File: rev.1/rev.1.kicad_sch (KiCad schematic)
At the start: 0 parts

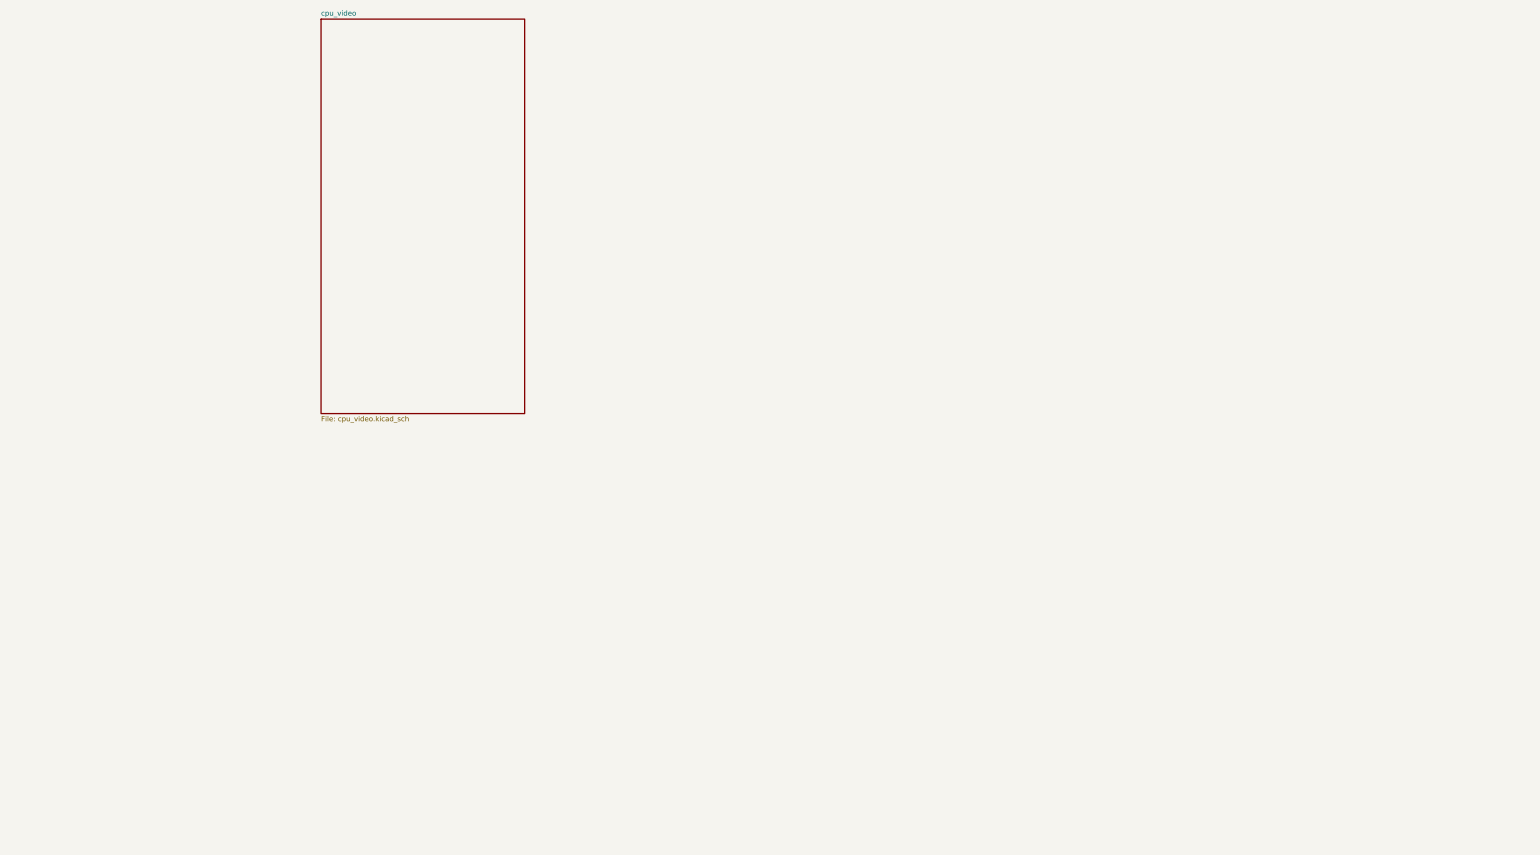
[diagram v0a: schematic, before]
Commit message: убрал иерархию
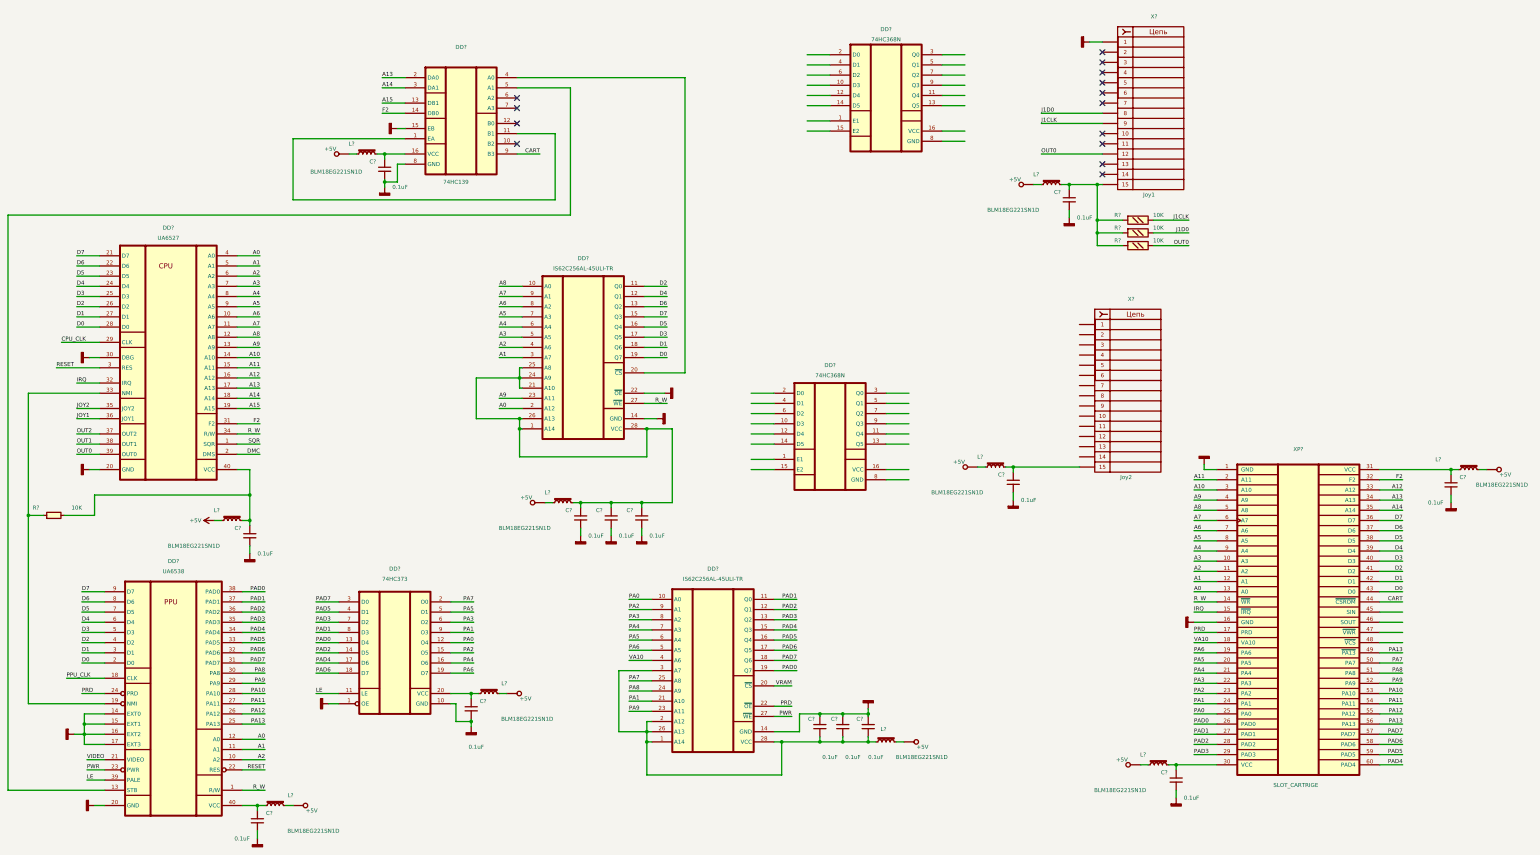
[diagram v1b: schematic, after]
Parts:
- added C? (x14): 0.1uF, symbol Device:C_Small
- added DD? (x2): 74HC368N, symbol 74xx:74HC368N_gost
- added DD? (x2): IS62C256AL-45ULI-TR, symbol Memory_RAM:IS62C256AL-45ULI-TR
- added DD?: 74HC373, symbol 74xx:74HC373_gost
- added DD?: 74HC139, symbol 74xx:74HC139N_gost
- added DD?: UA6527, symbol CPU:UA6527
- added DD?: UA6538, symbol Video:UA6538
- added L? (x10): BLM18EG221SN1D, symbol Device:L_Iron_Small
- added R? (x3): 10K, symbol Resistor_gost:R_125
- added R?: 10K, symbol Device:R_Small
- added X?: Joy1, symbol Connectors_gost:Conn_01x15_Female
- added X?: Joy2, symbol Connectors_gost:Conn_01x15_Female
- added XP?: SLOT_CARTRIGE, symbol Connector_Generic:Conn_02x30_Top_Bottom_dendy
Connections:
- new net: C?.1, C?.1, C?.1, DD?.1 (A14), DD?.21 (A10), DD?.24 (A9), DD?.25 (A8), DD?.26 (A13), DD?.28 (VCC), L?.2
- new net: DD?.20 (~{CS}), DD?.4 (A0)
- new net: C?.1, L?.2, R?.2, R?.2, R?.2, X?.15 (Pin_15)
- new net: C?.1, C?.1, C?.1, DD?.1 (A14), DD?.2 (A12), DD?.26 (A13), DD?.28 (VCC), DD?.3 (A7), L?.2
- new net: C?.1, DD?.16 (VCC), L?.2
- new net: C?.1, DD?.20 (VCC), L?.2
- new net: C?.1, DD?.40 (VCC), L?.2, R?.2
- new net: C?.1, L?.2, X?.15 (Pin_15)
- new net: C?.1, L?.2, XP?.31 (VCC)
- new net: C?.1, DD?.40 (VCC), L?.2
- new net: DD?.1 (EA), DD?.11 (B1)
- new net: DD?.13 (STB), DD?.5 (A1)
- new net: C?.1, L?.2, XP?.30 (VCC)
- new net: DD?.19 (NMI), DD?.33 (NMI), R?.1
- new net +5V: L?.1, L?.1, L?.1, L?.1, L?.1, L?.1, L?.1, L?.1, L?.1, L?.1
- new net A0: DD?.12 (A0), DD?.2 (A12), DD?.4 (A0), XP?.13 (A0)
- new net A1: DD?.11 (A1), DD?.3 (A7), DD?.5 (A1), XP?.12 (A1)
- new net A10: DD?.14 (A10), XP?.3 (A10)
- new net A11: DD?.15 (A11), XP?.2 (A11)
- new net A12: DD?.16 (A12), XP?.33 (A12)
- new net A13: DD?.17 (A13), DD?.2 (DA0), XP?.34 (A13)
- new net A14: DD?.18 (A14), DD?.3 (DA1), XP?.35 (A14)
- new net A15: DD?.13 (DB1), DD?.19 (A15)
- new net A2: DD?.10 (A2), DD?.4 (A6), DD?.6 (A2), XP?.11 (A2)
- new net A3: DD?.5 (A5), DD?.7 (A3), XP?.10 (A3)
- new net A4: DD?.6 (A4), DD?.8 (A4), XP?.9 (A4)
- new net A5: DD?.7 (A3), DD?.9 (A5), XP?.8 (A5)
- new net A6: DD?.10 (A6), DD?.8 (A2), XP?.7 (A6)
- new net A7: DD?.11 (A7), DD?.9 (A1), XP?.6 (A7)
- new net A8: DD?.10 (A0), DD?.12 (A8), XP?.5 (A8)
- new net A9: DD?.13 (A9), DD?.23 (A11), XP?.4 (A9)
- new net CART: DD?.9 (B3), XP?.44 (~{CSROM})
- new net CPU_CLK: DD?.29 (CLK)
- new net D0: DD?.19 (Q7), DD?.2 (D0), DD?.28 (D0), XP?.43 (D0)
- new net D1: DD?.18 (Q6), DD?.27 (D1), DD?.3 (D1), XP?.42 (D1)
- new net D2: DD?.11 (Q0), DD?.26 (D2), DD?.4 (D2), XP?.41 (D2)
- new net D3: DD?.17 (Q5), DD?.25 (D3), DD?.5 (D3), XP?.40 (D3)
- new net D4: DD?.12 (Q1), DD?.24 (D4), DD?.6 (D4), XP?.39 (D4)
- new net D5: DD?.16 (Q4), DD?.23 (D5), DD?.7 (D5), XP?.38 (D5)
- new net D6: DD?.13 (Q2), DD?.22 (D6), DD?.8 (D6), XP?.37 (D6)
- new net D7: DD?.15 (Q3), DD?.21 (D7), DD?.9 (D7), XP?.36 (D7)
- new net DMC: DD?.2 (DMS)
- new net F2: DD?.14 (DB0), DD?.31 (F2), XP?.32 (F2)
- new net GNDD: C?.2, C?.2, C?.2, C?.2, C?.2, C?.2, C?.2, C?.2, C?.2, C?.2, C?.2, C?.2, C?.2, C?.2, DD?.1 (OE), DD?.10 (GND), DD?.14 (EXT0), DD?.14 (GND), DD?.14 (GND), DD?.15 (EB), DD?.15 (EXT1), DD?.16 (EXT2), DD?.17 (EXT3), DD?.20 (GND), DD?.20 (GND), DD?.22 (~{OE}), DD?.30 (DBG), DD?.8 (GND), X?.1 (Pin_1), XP?.1 (GND), XP?.16 (GND)
- new net IRQ: DD?.32 (IRQ), XP?.15 (~{IRQ})
- new net J1CLK: R?.1, X?.9 (Pin_9)
- new net J1D0: R?.1, X?.8 (Pin_8)
- new net JOY1: DD?.36 (JOY1)
- new net JOY2: DD?.35 (JOY2)
- new net LE: DD?.11 (LE), DD?.39 (PALE)
- new net OUT0: DD?.39 (OUT0), R?.1, X?.12 (Pin_12)
- new net OUT1: DD?.38 (OUT1)
- new net OUT2: DD?.37 (OUT2)
- new net PA0: DD?.10 (A0), DD?.12 (O4), XP?.25 (PA0)
- new net PA1: DD?.21 (A10), DD?.9 (O3), XP?.24 (PA1)
- new net PA10: DD?.28 (PA10), XP?.53 (PA10)
- new net PA11: DD?.27 (PA11), XP?.54 (PA11)
- new net PA12: DD?.26 (PA12), XP?.55 (PA12)
- new net PA13: DD?.25 (PA13), XP?.49 (~{PA13}), XP?.56 (PA13)
- new net PA2: DD?.15 (O5), DD?.9 (A1), XP?.23 (PA2)
- new net PA3: DD?.6 (O2), DD?.8 (A2), XP?.22 (PA3)
- new net PA4: DD?.16 (O6), DD?.7 (A3), XP?.21 (PA4)
- new net PA5: DD?.5 (O1), DD?.6 (A4), XP?.20 (PA5)
- new net PA6: DD?.19 (O7), DD?.5 (A5), XP?.19 (PA6)
- new net PA7: DD?.2 (O0), DD?.25 (A8), XP?.50 (PA7)
- new net PA8: DD?.24 (A9), DD?.30 (PA8), XP?.51 (PA8)
- new net PA9: DD?.23 (A11), DD?.29 (PA9), XP?.52 (PA9)
- new net PAD0: DD?.13 (D4), DD?.19 (Q7), DD?.38 (PAD0), XP?.26 (PAD0)
- new net PAD1: DD?.11 (Q0), DD?.37 (PAD1), DD?.8 (D3), XP?.27 (PAD1)
- new net PAD2: DD?.12 (Q1), DD?.14 (D5), DD?.36 (PAD2), XP?.28 (PAD2)
- new net PAD3: DD?.13 (Q2), DD?.35 (PAD3), DD?.7 (D2), XP?.29 (PAD3)
- new net PAD4: DD?.15 (Q3), DD?.17 (D6), DD?.34 (PAD4), XP?.60 (PAD4)
- new net PAD5: DD?.16 (Q4), DD?.33 (PAD5), DD?.4 (D1), XP?.59 (PAD5)
- new net PAD6: DD?.17 (Q5), DD?.18 (D7), DD?.32 (PAD6), XP?.58 (PAD6)
- new net PAD7: DD?.18 (Q6), DD?.3 (D0), DD?.31 (PAD7), XP?.57 (PAD7)
- new net PPU_CLK: DD?.18 (CLK)
- new net PRD: DD?.22 (~{OE}), DD?.24 (PRD), XP?.17 (PRD)
- new net PWR: DD?.23 (PWR), DD?.27 (~{WE})
- new net RESET: DD?.22 (RES), DD?.3 (RES)
- new net R_W: DD?.1 (R/W), DD?.27 (~{WE}), DD?.34 (R/W), XP?.14 (~{WR})
- new net SQR: DD?.1 (SQR)
- new net VA10: DD?.4 (A6), XP?.18 (VA10)
- new net VIDEO: DD?.21 (VIDEO)
- new net VRAM: DD?.20 (~{CS})
- no-connect marks 0 -> 14
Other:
- removed sheet cpu_video

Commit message: добавил документацию опринципах работы приставки и доделал джойстики
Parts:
- removed C?: 0.1uF, symbol Device:C_Small
- removed L?: BLM18EG221SN1D, symbol Device:L_Iron_Small
- removed R? (x2): 10K, symbol Resistor_gost:R_125
- removed X?: Joy1, symbol Connectors_gost:Conn_01x15_Female
- removed X?: Joy2, symbol Connectors_gost:Conn_01x15_Female
- added C? (x3): 0.1uF, symbol Device:C_Small
- added L? (x3): BLM18EG221SN1D, symbol Device:L_Iron_Small
- added R? (x11): 10K, symbol Resistor_gost:R_125
- added X?: Манипулятор_2, symbol Connectors_gost:DB15_Female_HighDensity_gost
- added X?: Манипулятор_1, symbol Connectors_gost:DB15_Female_HighDensity_gost
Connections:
- net +5V: now also L?.1, L?.1, L?.1
- net D0: now also DD?.13 (Q5), DD?.3 (Q0)
- net D1: now also DD?.5 (Q1), DD?.5 (Q1)
- net D2: now also DD?.11 (Q4), DD?.9 (Q3)
- net D3: now also DD?.7 (Q2)
- net D4: now also DD?.9 (Q3)
- net F2: now also DD?.2 (D0), DD?.6 (D2)
- net GNDD: now also DD?.10 (D3), DD?.15 (E2), DD?.8 (GND), DD?.8 (GND), C?.2, C?.2, C?.2, X?.1, X?.1
- net IRQ: now also R?.1, X?.3
- net J1CLK: now also DD?.7 (Q2), R?.1, X?.14, X?.9; no longer R?.1
- net J1D0: now also DD?.2 (D0), R?.1, X?.2, X?.8
- net JOY1: now also DD?.1 (E1)
- net JOY2: now also DD?.1 (E1), DD?.15 (E2)
- net OUT0: now also R?.1, X?.12, X?.12
- net OUT1: now also R?.1, X?.11
- net OUT2: now also R?.1, X?.10
- net PA13: now also DD?.12 (D4); no longer XP?.49 (~{PA13})
- net PWR: now also XP?.47 (~{VWR})
- net VRAM: now also XP?.48 (~{VCS})
- net nPA13: now reaches DD?.11 (Q4)
- net nPA13: now also XP?.49 (~{PA13})
- net at DD?.16 (VCC): now also C?.1, L?.2 (x2)
- net J1D1: now reaches DD?.4 (D1)
- net J1D1: now also X?.13
- net at C?.1, L?.2, R?.2: now also R?.2, R?.2, X?.15
- net J2D4: now reaches DD?.10 (D3)
- net J2D4: now also R?.1, X?.4
- net J2D2: now reaches DD?.12 (D4)
- net J2D2: now also R?.1, X?.6
- net J2D0: now reaches DD?.14 (D5)
- net J2D0: now also R?.1, X?.8
- net J2CLK: now reaches DD?.3 (Q0)
- net J2CLK: now also R?.1, X?.9
- net J2D1: now reaches DD?.4 (D1)
- net J2D1: now also R?.1, X?.7
- net J2D3: now reaches DD?.6 (D2)
- net J2D3: now also R?.1, X?.5
- net at XP?.45 (SIN): now also XP?.46 (SOUT)
- new net: C?.1, L?.2, R?.2, R?.2, R?.2, R?.2, R?.2, R?.2, R?.2, R?.2, R?.2, X?.15
- no-connect marks 14 -> 6
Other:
- moved on the sheet: C?, DD?, L?, R?, XP?

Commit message: добавил видеоусилитель
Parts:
- added C?: 220uFx10V, symbol Device_gost:C_Polarized_Small
- added C? (x10): 330pF, symbol Device:C_Small
- added C?: 0.1uF, symbol Device:C_Small
- added D?: SS14, Diode_SMD_AKL:D_SMA, symbol Diode_Schottky_gost:SS14
- added L?: BLM18EG221SN1D, symbol Device:L_Iron_Small
- added Q?: BC817, Package_TO_SOT_SMD:SOT-23, symbol Transistor_BJT:BC817
- added Q?: BC857, Package_TO_SOT_SMD:SOT-23, symbol Transistor_BJT:BC857
- added R?: 75R, symbol Resistor_gost:R_125
- added R?: 2K2, symbol Resistor_gost:R_125
- added R?: 220R, symbol Resistor_gost:R_125
- added R?: 68R, symbol Resistor_gost:R_125
- added X?: VIDEO, symbol Connectors_gost:Conn_01x04_Female
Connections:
- net +5V: now also L?.1
- net GNDD: now also C?.2, C?.2, C?.2, C?.2, C?.2, C?.2, C?.2, C?.2, C?.2, C?.2, C?.2, Q?.3 (C), R?.1, X?.2 (Pin_2), X?.3 (Pin_3), X?.4 (Pin_4)
- net IRQ: now also C?.1
- net J1CLK: now also C?.1
- net J1D0: now also C?.1
- net J2CLK: now also C?.1
- net J2D0: now also C?.1
- net J2D1: now also C?.1
- net J2D2: now also C?.1
- net J2D3: now also C?.1
- net J2D4: now also C?.1
- net OUT2: now also C?.1
- net VIDEO: now also Q?.1 (B)
- new net: D?.1 (K), Q?.1 (B), R?.1, R?.2
- new net: C?.1, D?.2 (A), Q?.2 (E), R?.2
- new net: C?.2, R?.2
- new net: R?.1, X?.1 (Pin_1)
- new net: C?.1, L?.2, Q?.3 (C), R?.2
- new net: Q?.2 (E), R?.1
- no-connect marks 6 -> 16
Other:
- note added: "ВЫХОД"
- note added: "ЗЕМЛЯ"
- moved on the sheet: C?, L?, XP?

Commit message: добавил генератор частоты на 74ls04
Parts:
- added C?: 0.1uF, symbol Device:C_Small
- added C? (x2): 22pF, symbol Device:C_Small
- added DD?: 74LS04, symbol 74xx:74HC04_gost
- added L?: BLM18EG221SN1D, symbol Device:L_Iron_Small
- added R?: 4M7, symbol Resistor_gost:R_125
- added Z?: 26.601712 Mhz, symbol Device_gost:Crystal_Small
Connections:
- net +5V: now also L?.1
- net CPU_CLK: now also DD?.6 (3Y)
- net GNDD: now also C?.2, C?.2, C?.2, DD?.11 (5A), DD?.13 (6A), DD?.7 (GND), DD?.9 (4A)
- net PPU_CLK: now also DD?.4 (2Y)
- new net: C?.1, DD?.10 (5Y), DD?.12 (6Y), DD?.14 (VCC), DD?.8 (4Y), L?.2
- new net: C?.1, DD?.1 (1A), R?.2, Z?.1
- new net: C?.1, DD?.2 (1Y), DD?.3 (2A), DD?.5 (3A), R?.1, Z?.2

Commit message: закончил схему звукового вывода
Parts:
- added C? (x2): 0.1uF, symbol Device:C_Small
- added C? (x5): 10uFx16V, symbol Device_gost:C_Polarized_Small
- added DA? (x2): LM358, symbol Amplifier_Operational:LM2904_gost
- added L?: BLM18EG221SN1D, symbol Device:L_Iron_Small
- added R? (x6): 4K7, symbol Resistor_gost:R_125
- added R? (x2): 75R, symbol Resistor_gost:R_125
- added R? (x2): 1R, symbol Resistor_gost:R_125
- added R? (x2): 510R, symbol Resistor_gost:R_125
- added R? (x3): 1K, symbol Resistor_gost:R_125
- added R? (x2): 2K, symbol Resistor_gost:R_125
- added R?: 1K8, symbol Resistor_gost:R_125
- added R? (x2): 10K, symbol Resistor_gost:R_125
- added R?: 2K2, symbol Resistor_gost:R_125
- added X?: AUDIO_1, symbol Connectors_gost:Conn_01x04_Female
- added X?: AUDIO_2, symbol Connectors_gost:Conn_01x04_Female
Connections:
- net +5V: now also L?.1
- net DMC: now also R?.1, R?.2, R?.2
- net GNDD: now also C?.2, C?.2, C?.2, DA?.4 (V-), R?.1, R?.1, R?.1, R?.2, R?.2, R?.2, X?.2 (Pin_2), X?.2 (Pin_2), X?.3 (Pin_3), X?.3 (Pin_3), X?.4 (Pin_4), X?.4 (Pin_4)
- net SQR: now also R?.1, R?.2, R?.2
- net SOUT: now reaches XP?.45 (SIN), XP?.46 (SOUT)
- net SOUT: now also R?.1, R?.2, R?.2
- new net: C?.2, R?.1, R?.1, R?.1 (x2)
- new net: C?.1, R?.1 (x2)
- new net: DA?.7, R?.1, R?.2
- new net: C?.1, C?.1, R?.1, R?.2, R?.2, R?.2
- new net: C?.2, X?.1 (Pin_1) (x2)
- new net: DA?.6 (-), R?.1, R?.2
- new net: C?.1, DA?.5 (+), R?.1, R?.2
- new net: C?.1, DA?.3 (+), R?.1, R?.2
- new net: DA?.1, R?.1, R?.2
- new net: DA?.2 (-), R?.1, R?.2
- new net +5VA: C?.1, DA?.8 (V+), L?.2, R?.2, R?.2, R?.2
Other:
- moved on the sheet: C?, D?, DD?, L?, Q?, R?, X?, Z?

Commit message: Добавил стабилизатор питания и закончил схему
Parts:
- added C1: 0.47uF, symbol Device:C_Small
- added C2: 220uFx25V, symbol Device_gost:C_Polarized_Small
- added C6: 470p, symbol Device:C_Small
- added C8: 470uFx6.3V, symbol Device_gost:C_Polarized_Small
- added D1, D2: SS14, Diode_SMD_AKL:D_SMA, symbol Diode_Schottky_gost:SS14
- added D3: POWER, symbol Device:LED_Small
- added DA1: MC34063AD, Package_SO:SOIC-8_3.9x4.9mm_P1.27mm, symbol Regulator_Switching:MC33063AD
- added L4: 220uH, symbol Device_gost:L_Ferrite_Small
- added R1: 10K, symbol Device:R_Small
- added R3: 0.12R, symbol Device:R_Small
- added R4: 3K6, symbol Device:R_Small
- added R5: 1K2, symbol Device:R_Small
- added R6: 330R, symbol Device:R_Small
- added SW1: RESET, symbol Switch:SW_Push_Dual
- added SW2: POWER, symbol Switch:SW_Push_Dual
- added X1: POWER, symbol Connectors_gost:Conn_01x03_Female
- gave numbers to parts that had none: 112
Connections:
- net +5V: now also C8.1, L4.2, R1.2, R4.2, R6.2
- net GNDD: now also C1.2, C2.2, C6.2, C8.2, D2.2 (A), D3.1 (K), DA1.4 (GND), R5.1, SW1.1, SW1.3, X1.2 (Pin_2), X1.3 (Pin_3)
- net RESET: now also C1.1, R1.1, SW1.2, SW1.4
- new net: D1.1 (K), SW2.1, SW2.3
- new net: D1.2 (A), X1.1 (Pin_1)
- new net: D3.2 (A), R6.1
- new net: C2.1, DA1.6 (Vin), R3.1, SW2.2, SW2.4
- new net: DA1.1 (SwC), DA1.7 (Ipk), DA1.8 (DC), R3.2
- new net: D2.1 (K), DA1.2 (SwE), L4.1
- new net: C6.1, DA1.3 (TC)
- new net: DA1.5 (Vfb), R4.1, R5.2
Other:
- note added: "GND"
- note added: "VCC+"

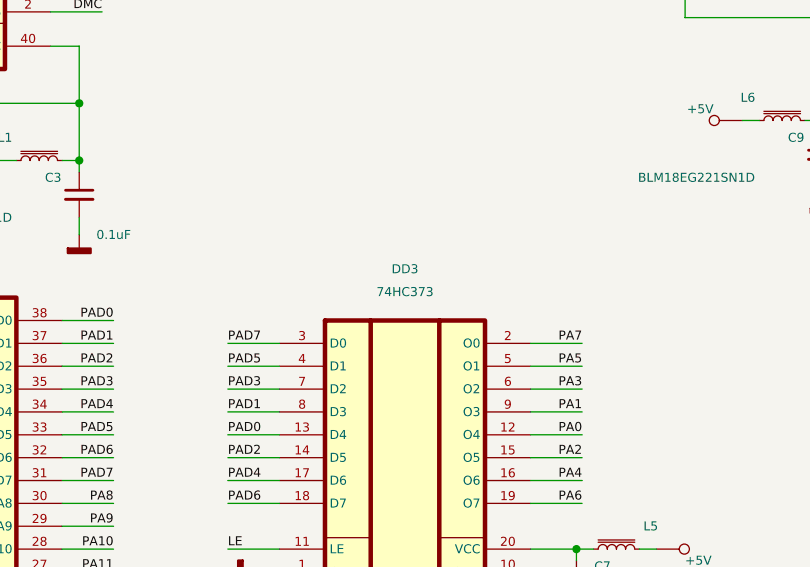
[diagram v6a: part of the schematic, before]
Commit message: сделал контур платы  и начал раставлять элементц
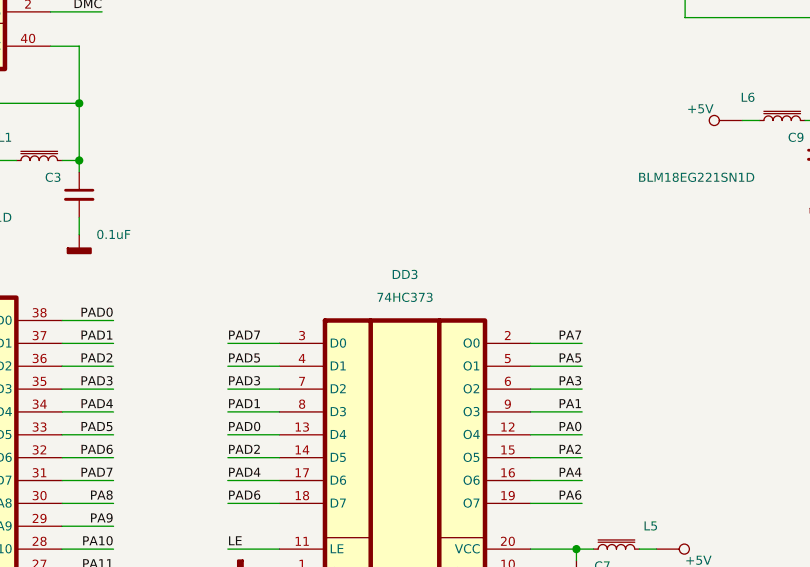
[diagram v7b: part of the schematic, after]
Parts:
- C1, C10, C11, C12, C13, C14, C15, C16, C17, C18, C19, C20, C23, C24, C25, C27, C28, C29, C3, C30, C31, C32, C33, C36, C37, C38, C4, C40, C41, C42, C5, C6, C7, C9: footprint (none) -> Capacitor_SMD:C_0603_1608Metric
- C2: footprint (none) -> Capacitor_THT:CP_Radial_D10.0mm_P5.00mm
- C21, C22, C26, C34, C35, C8: footprint (none) -> Capacitor_THT:CP_Radial_D6.3mm_P2.50mm
- C39: footprint (none) -> Capacitor_THT:CP_Radial_D7.5mm_P2.50mm
- D1, D2, D4: footprint Diode_SMD_AKL:D_SMA -> Diode_SMD:D_SMA
- D3: footprint (none) -> LED_THT:LED_D3.0mm
- DA2: footprint (none) -> Package_SO:SOIC-8_3.9x4.9mm_P1.27mm
- DD1, DD2: footprint (none) -> Package_DIP:DIP-40_W15.24mm_Socket
- DD3: footprint (none) -> Package_SO:SO-20_12.8x7.5mm_P1.27mm
- DD4, DD7, DD8: footprint (none) -> Package_SO:SO-16_3.9x9.9mm_P1.27mm
- DD5, DD6: footprint (none) -> Package_SO:SOIC-28W_7.5x17.9mm_P1.27mm
- DD9: footprint (none) -> Package_SO:SO-14_3.9x8.65mm_P1.27mm
- L1, L10, L11, L12, L13, L14, L15, L16, L2, L3, L5, L6, L7, L8, L9: footprint (none) -> Inductor_SMD:L_0603_1608Metric
- L4: footprint (none) -> Inductor_THT:L_Radial_D7.0mm_P3.00mm
- R1, R10, R11, R12, R13, R14, R15, R16, R17, R18, R19, R2, R20, R21, R22, R23, R24, R25, R26, R27, R28, R29, R3, R30, R31, R32, R33, R34, R35, R36, R37, R38, R39, R4, R40, R41, R42, R43, R44, R5, R6, R7, R8, R9: footprint (none) -> Resistor_SMD:R_0603_1608Metric
- SW1: footprint (none) -> Button_Switch_THT:SW_PUSH_6mm_H7.3mm
- SW2: footprint (none) -> Button_Switch_THT:Nidec_Copal_SH-7010C
- X1: footprint (none) -> Connector_BarrelJack:BarrelJack_Wuerth_6941xx301002
- X2, X5: footprint (none) -> Connector_Dsub:DSUB-15_Male_Horizontal_P2.77x2.84mm_EdgePinOffset4.94mm_Housed_MountingHolesOffset7.48mm
- X3, X4, X6: footprint (none) -> Connector_Audio:rca_red
- XP1: footprint (none) -> Connector:60 PIN FAMICOM CARTRIDGE SLOT
- Z1: footprint (none) -> Crystal:Crystal_SMD_HC49-SD
